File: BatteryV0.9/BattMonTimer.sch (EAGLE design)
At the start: 62 parts, among them IC1 TMP36GT9Z, IC2 TLV2211, IC3 INA138, IC4 TMP36GRT, IC6 CD74HC4060, IC7 74LVC1G74DCT, IC8 ICM7555SO08, M1 Mount, M2 Mount, P2 SSM3J338RSOT-23F_TOS-M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

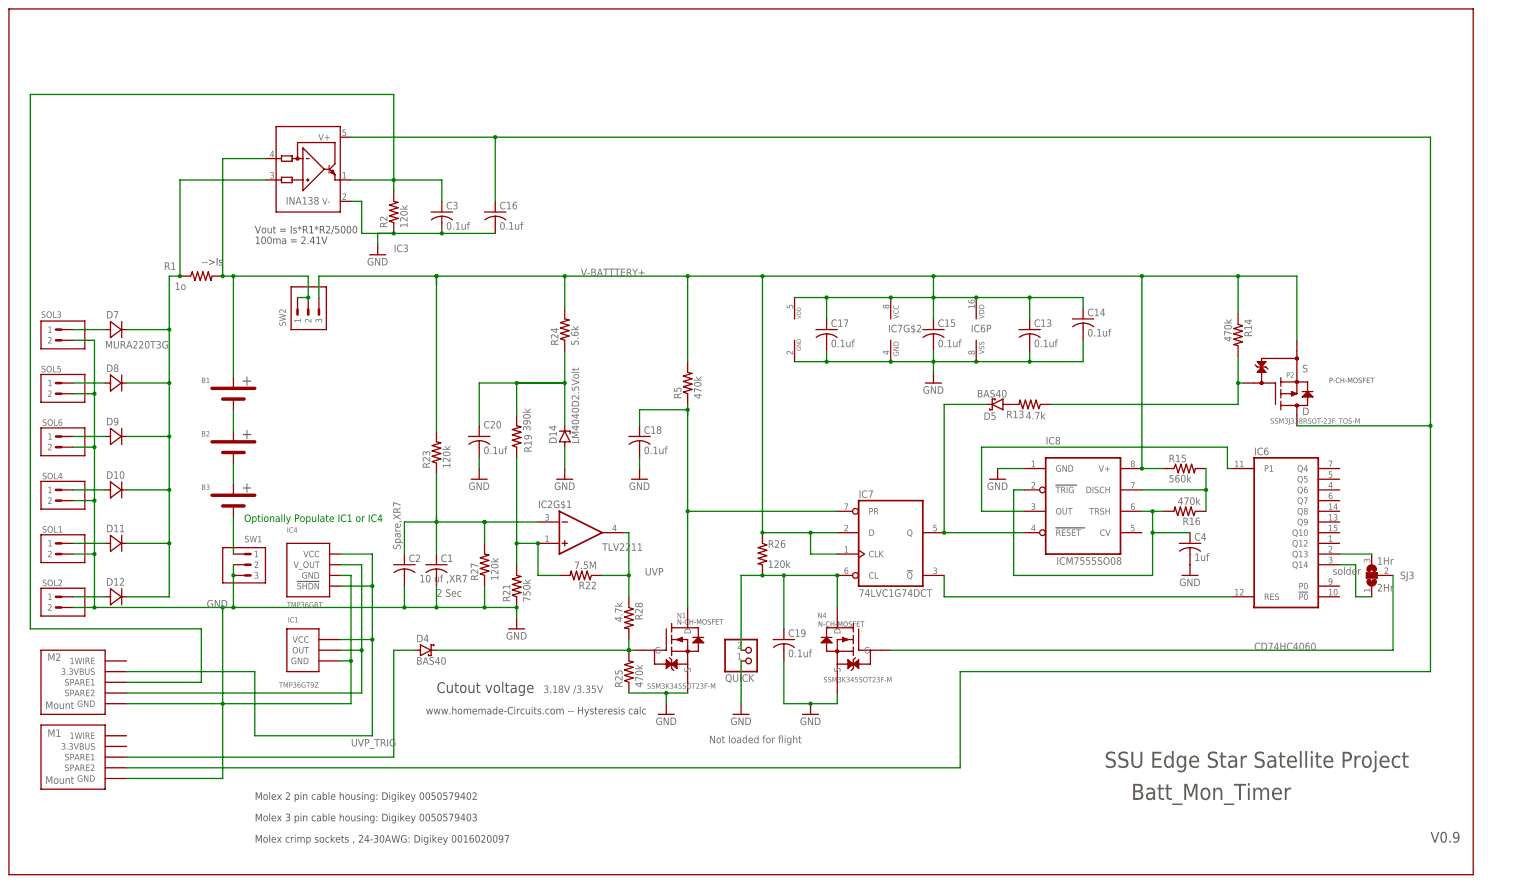
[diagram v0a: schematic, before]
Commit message: 
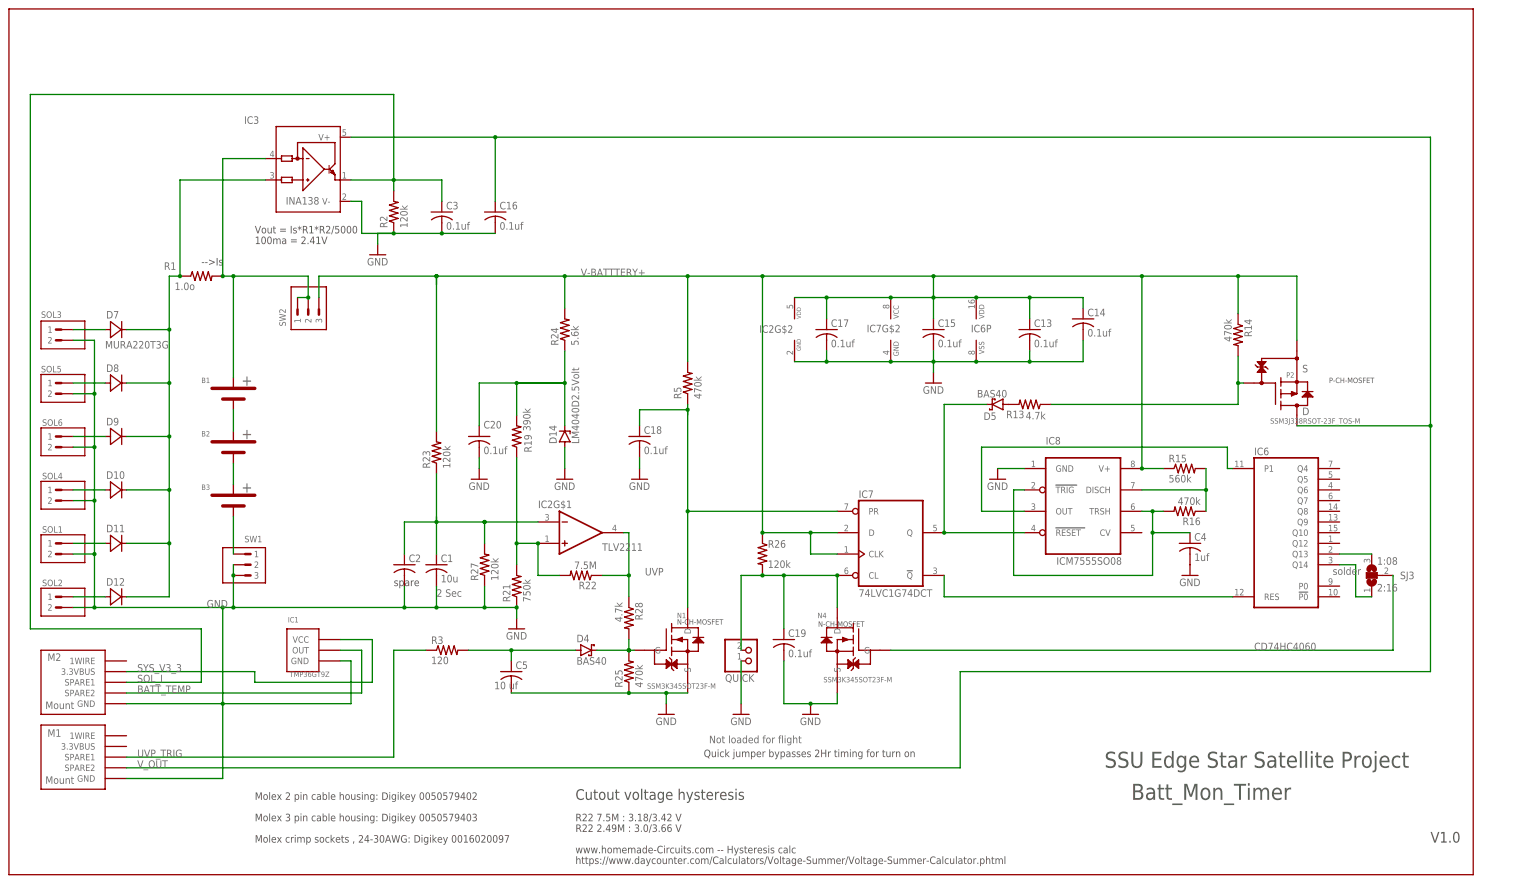
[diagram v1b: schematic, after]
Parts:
- removed IC4: TMP36GRT, BattMonTimer:TMP36GRT
- added C5: 10 uf, rcl:C-USC0805
- added R3: 120, rcl:R-US_R0805
- C1: value 10 uf ,XR7 -> 10u
- C2: value Spare,XR7 -> (none)
- R1: value 1o -> 1.0o
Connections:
- net N$38 renamed V_OUT
- net SOL_CURRENT renamed SOL_I
- removed net N$2: IC1.OUT, IC4.V_OUT, M2.SPARE2
- removed net N$3: IC1.VCC, IC4.!SHDN, IC4.VCC, M2.3.3VBUS
- new net BATT_TEMP: IC1.OUT, M2.SPARE2
- new net N$5: C5.1, D4.A, R3.2
- new net SYS_V3_3: IC1.VCC, M2.3.3VBUS
- net GND: now also C5.2; no longer IC4.GND
- net UVP_TRIG: now also R3.1; no longer D4.A
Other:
- note added: "1:08"
- note added: "2:16"
- note added: "Cutout voltage hysteresis"
- note added: "Quick jumper bypasses 2Hr timing for turn on"
- note added: "R22 2.49M : 3.0/3.66 V"
- note added: "R22 7.5M : 3.18/3.42 V"
- note added: "V1.0"
- note added: "https://www.daycounter.com/Calculators/Voltage-Summer/Voltage-Summer-Calculator.phtml"
- note added: "spare"
- note removed: "1Hr"
- note removed: "2Hr"
- note removed: "3.18V /3.35V"
- note removed: "Cutout voltage"
- note removed: "Optionally Populate IC1 or IC4"
- note removed: "V0.9"
- moved on the sheet: D4
